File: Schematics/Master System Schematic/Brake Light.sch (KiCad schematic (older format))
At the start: 4 parts, among them U13 CAN_Bus_Module, U15 KY-019, U8 SD_Card_Module

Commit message: Missing annotation
Annotated MC resistor
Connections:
- new net: A3.~ (~~D9), U13.~ (Serial_Clock), U15.2 (+), U8.~ (VCC)
- new net: A3.~ (~~D9), U13.~ (Serial_Clock)
- new net: A3.~ (~~D9), U13.~ (Serial_Clock), U8.~ (VCC) (x4)
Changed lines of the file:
@@
 $Descr A 11000 8500
 encoding utf-8
-Sheet 18 22
+Sheet 17 22
 Title "Brake Light CAN Box"
 Date "2020-11-01"

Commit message: Continued VPM Board integration
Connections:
- new net: A3.~ (~~D9), U13.~ (Serial_Clock), U15.2 (+), U8.~ (VCC)
- new net: A3.~ (~~D9), U13.~ (Serial_Clock)
- new net: A3.~ (~~D9), U13.~ (Serial_Clock), U8.~ (VCC) (x4)
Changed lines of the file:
@@
 $Descr A 11000 8500
 encoding utf-8
-Sheet 17 22
+Sheet 17 23
 Title "Brake Light CAN Box"
 Date "2020-11-01"

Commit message: Added/Fixed Sheet Connections Within BMS Container
> Added hierarchical labels for each input on the VPM and connected them to hierarchical labels and the BMS within the BMS container.
> Added CANS(Charger) hierarchical label coming out of the BMS container sheet and connected it to the charger CAN bus line.

BMS Container Version 8.1
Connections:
- new net: A3.~ (~~D9), U13.~ (Serial_Clock), U15.2 (+), U8.~ (VCC)
- new net: A3.~ (~~D9), U13.~ (Serial_Clock)
- new net: A3.~ (~~D9), U13.~ (Serial_Clock), U8.~ (VCC) (x4)
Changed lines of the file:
@@
 EESchema Schematic File Version 4
-LIBS:Master System Schematic-cache
 EELAYER 30 0
 EELAYER END

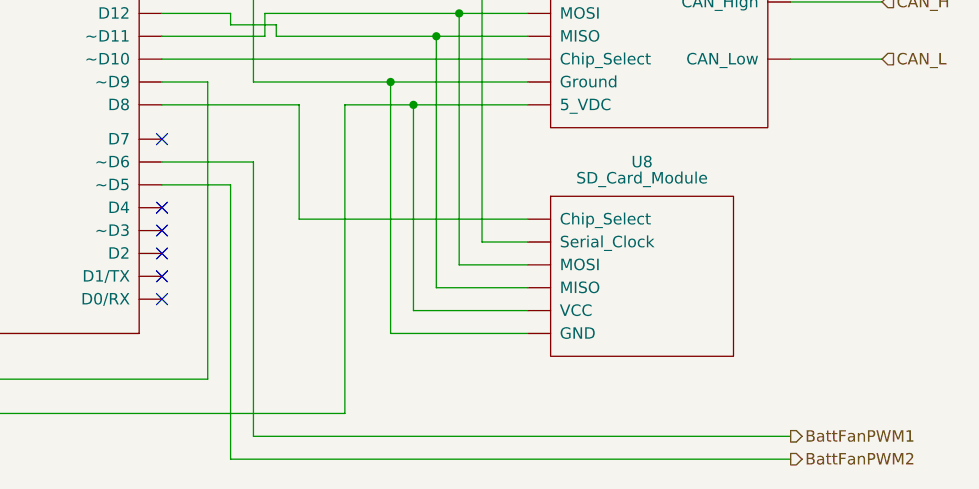
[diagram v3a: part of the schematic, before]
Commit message: Master Schematic and VPM Changes
> Thermal Expansion and Critical Therm busses combined into Temperature_Data in Accumulator_Container.sch
> BattFanPWM added to Temperature_Data connector
> PumpIO connector changed from 2 to 4 pins
> Added 7-Pin Generic connector
> Updated VPM board schematic

VPM Version 5
Master Schematic Version 14.1
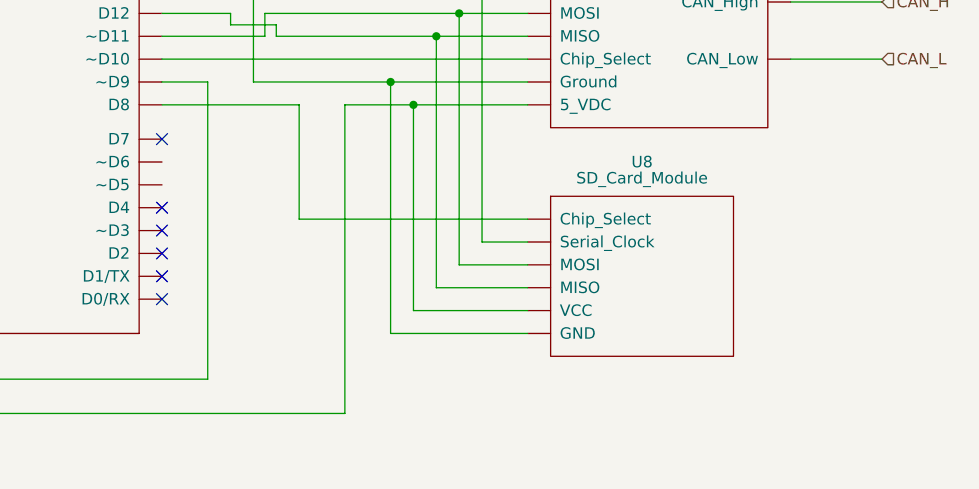
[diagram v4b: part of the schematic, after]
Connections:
- net BattFanPWM1 is gone; now on net CAN_SHIELD: A3.~ (~~D9)
- net BattFanPWM2 is gone; now on net CAN_SHIELD: A3.~ (~~D9)
- new net: A3.~ (~~D9), U13.~ (Serial_Clock), U15.2 (+), U8.~ (VCC)
- new net: A3.~ (~~D9), U13.~ (Serial_Clock)
- new net: A3.~ (~~D9), U13.~ (Serial_Clock), U8.~ (VCC) (x4)
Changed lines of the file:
@@
 Text HLabel 3350 3950 0    50   Input ~ 0
 CAN_SHIELD
-Wire Wire Line
-	5700 5400 8050 5400
-Text HLabel 8050 5400 2    50   Output ~ 0
-BattFanPWM1
-Text HLabel 8050 5500 2    50   Output ~ 0
-BattFanPWM2
 $Comp
 L NER:CAN_Bus_Module U13
@@
 Wire Wire Line
 	5900 4450 6900 4450
-Wire Wire Line
-	5700 5400 5700 4200
-Wire Wire Line
-	5700 4200 5300 4200
-Wire Wire Line
-	8050 5500 5600 5500
-Wire Wire Line
-	5600 5500 5600 4300
-Wire Wire Line
-	5600 4300 5300 4300
 $Comp
 L NER:SD_Card_Module U8

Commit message: HV Plate
> Added HV_Plate, LV_Plate, and Segment_Layer subsheets to batbox
> Recreated current HV circuit in HV_Plate sheet
> Added placeholders for HV_Plate wire sizes
> Added outputs in HV_Plate sheet
> Added component datasheets for HV circuit

HV_Plate V1.0
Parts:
- A3: symbol NER:Arduino_UNO_rev3 -> Master-System-Schematic-rescue:Arduino_UNO_rev3-NER
- U13: symbol NER:CAN_Bus_Module -> Master-System-Schematic-rescue:CAN_Bus_Module-NER
- U15: symbol NER:KY-019 -> Master-System-Schematic-rescue:KY-019-NER
- U8: symbol NER:SD_Card_Module -> Master-System-Schematic-rescue:SD_Card_Module-NER
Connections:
- new net: A3.~ (~~D9), U13.~ (Serial_Clock), U15.2 (+), U8.~ (VCC)
- new net: A3.~ (~~D9), U13.~ (Serial_Clock)
- new net: A3.~ (~~D9), U13.~ (Serial_Clock), U8.~ (VCC) (x4)
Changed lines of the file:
@@
 $Descr A 11000 8500
 encoding utf-8
-Sheet 17 23
+Sheet 17 26
 Title "Brake Light CAN Box"
 Date "2020-11-01"
@@
 $EndDescr
 $Comp
-L NER:KY-019 U15
+L Master-System-Schematic-rescue:KY-019-NER U15
 U 1 1 5F8C06C7
 P 4700 1950
@@
 NoConn ~ 4100 3750
 $Comp
-L NER:Arduino_UNO_rev3 A3
+L Master-System-Schematic-rescue:Arduino_UNO_rev3-NER A3
 U 1 1 5F8BEBC7
 P 4700 2700
@@
 CAN_SHIELD
 $Comp
-L NER:CAN_Bus_Module U13
+L Master-System-Schematic-rescue:CAN_Bus_Module-NER U13
 U 1 1 5F8C522E
 P 7450 3200
@@
 	5900 4450 6900 4450
 $Comp
-L NER:SD_Card_Module U8
+L Master-System-Schematic-rescue:SD_Card_Module-NER U8
 U 1 1 6053C07D
 P 7400 4250

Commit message: Segment Layer
> Added segments to Segment_Layer sheet
> Added VT PCBs and Thermistor PCBs to Segment_Layer sheet
> Removed relays from VT PCBs
> Still need to add connectors to VT and Thermistor PCBs once PCBs have been redesigned
> Added outputs for Segment_Layer sheet
> Added wire gauges to Segment_Layer sheet

Segment_Layer V1.0
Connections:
- new net: A3.~ (~~D9), U13.~ (Serial_Clock), U15.2 (+), U8.~ (VCC)
- new net: A3.~ (~~D9), U13.~ (Serial_Clock)
- new net: A3.~ (~~D9), U13.~ (Serial_Clock), U8.~ (VCC) (x4)
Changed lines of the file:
@@
 $Descr A 11000 8500
 encoding utf-8
-Sheet 17 26
+Sheet 17 38
 Title "Brake Light CAN Box"
 Date "2020-11-01"

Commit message: LV Plate
> Added basic connectors and outlines for MCR PCB
> Added and wired components on LV Plate
> Added GLV connector
> Connected layers
> Some wire gauges still needed

LV_Plate Version 1.0
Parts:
- A3: symbol Master-System-Schematic-rescue:Arduino_UNO_rev3-NER -> NER:Arduino_UNO_rev3
- U13: symbol Master-System-Schematic-rescue:CAN_Bus_Module-NER -> NER:CAN_Bus_Module
- U15: symbol Master-System-Schematic-rescue:KY-019-NER -> NER:KY-019
- U8: symbol Master-System-Schematic-rescue:SD_Card_Module-NER -> NER:SD_Card_Module
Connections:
- new net: A3.~ (~~D9), U13.~ (Serial_Clock), U15.2 (+), U8.~ (VCC)
- new net: A3.~ (~~D9), U13.~ (Serial_Clock)
- new net: A3.~ (~~D9), U13.~ (Serial_Clock), U8.~ (VCC) (x4)
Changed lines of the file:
@@
 $Descr A 11000 8500
 encoding utf-8
-Sheet 17 38
+Sheet 17 40
 Title "Brake Light CAN Box"
 Date "2020-11-01"
@@
 $EndDescr
 $Comp
-L Master-System-Schematic-rescue:KY-019-NER U15
+L NER:KY-019 U15
 U 1 1 5F8C06C7
 P 4700 1950
@@
 NoConn ~ 4100 3750
 $Comp
-L Master-System-Schematic-rescue:Arduino_UNO_rev3-NER A3
+L NER:Arduino_UNO_rev3 A3
 U 1 1 5F8BEBC7
 P 4700 2700
@@
 CAN_SHIELD
 $Comp
-L Master-System-Schematic-rescue:CAN_Bus_Module-NER U13
+L NER:CAN_Bus_Module U13
 U 1 1 5F8C522E
 P 7450 3200
@@
 	5900 4450 6900 4450
 $Comp
-L Master-System-Schematic-rescue:SD_Card_Module-NER U8
+L NER:SD_Card_Module U8
 U 1 1 6053C07D
 P 7400 4250

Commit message: LV Plate Cleanup + Other Small Stuff
> Renamed MCR PCB to BattBox PCB
> Added 7 Pin IMD connector to BattBox PCB
> Fixed wire gauges on Segment Layer sheet
> Added HV cutout on LV Plate
> Added fan signals
> Deleted old accumulator stuff
> Added BattBox and BMS fans

BattBox PCB V1.0
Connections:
- new net: A3.~ (~~D9), U13.~ (Serial_Clock), U15.2 (+), U8.~ (VCC)
- new net: A3.~ (~~D9), U13.~ (Serial_Clock)
- new net: A3.~ (~~D9), U13.~ (Serial_Clock), U8.~ (VCC) (x4)
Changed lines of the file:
@@
 $Descr A 11000 8500
 encoding utf-8
-Sheet 17 40
+Sheet 17 27
 Title "Brake Light CAN Box"
 Date "2020-11-01"
